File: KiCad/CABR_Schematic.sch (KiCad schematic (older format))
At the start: 22 parts, among them J1 XT60 Connector, J2 0.1\" Header, M1 Solenoid, M2 Flywheel 1, M3 Flywheel 2, Q1 PBSS4250X, SW1 Fire Mode, SW2 Microswitch, SW3 Motor Spin Up, U1 AZ1117-5.0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

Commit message: got PCB design
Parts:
- removed J1: XT60 Connector, symbol Connector_Generic:Conn_01x02
- removed M2: Flywheel 1, symbol Motor:Motor_DC_ALT
- removed M3: Flywheel 2, symbol Motor:Motor_DC_ALT
- removed SW3: Motor Spin Up, symbol Switch:SW_Push_Open
- added C3: 0.1uF, Capacitor_SMD:C_0805_2012Metric, symbol Device:C
- added J1, J5: Screw_Terminal_01x02, XT60:XT60, symbol Connector:Screw_Terminal_01x02
- added J3: Program Header, Connector_PinHeader_2.54mm:PinHeader_2x03_P2.54mm_Vertical, symbol Connector_Generic:Conn_02x03_Top_Bottom
- added J4: MicroSwitch, Connector_PinHeader_2.54mm:PinHeader_1x02_P2.54mm_Vertical, symbol Connector:Conn_01x02_Male
- C1, C2: footprint (none) -> Capacitor_SMD:C_0805_2012Metric
- D1: footprint (none) -> LED_SMD:LED_0805_2012Metric
- D2: value 1N4148 -> MMSD4148T3G; footprint Diode_THT:D_DO-35_SOD27_P7.62mm_Horizontal -> Diode_SMD:D_SOD-123
- J2: footprint (none) -> Connector_PinHeader_2.54mm:PinHeader_1x03_P2.54mm_Vertical
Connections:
- wire segments 71 -> 82
- no-connect marks 6 -> 10
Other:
- moved on the sheet: M1, SW2
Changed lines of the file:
@@
 F 0 "C2" H 6318 1896 50  0000 L CNN
 F 1 "10uF" H 6318 1805 50  0000 L CNN
-F 2 "" H 6238 1700 50  0001 C CNN
+F 2 "Capacitor_SMD:C_0805_2012Metric" H 6238 1700 50  0001 C CNN
 F 3 "~" H 6200 1850 50  0001 C CNN
 	1    6200 1850
@@
 F 0 "C1" H 5418 1896 50  0000 L CNN
 F 1 "10uF" H 5418 1805 50  0000 L CNN
-F 2 "" H 5338 1700 50  0001 C CNN
+F 2 "Capacitor_SMD:C_0805_2012Metric" H 5338 1700 50  0001 C CNN
 F 3 "~" H 5300 1850 50  0001 C CNN
 	1    5300 1850
@@
 	7100 3150 7100 3900
 Wire Wire Line
-	6050 2750 6050 2950
-Wire Wire Line
-	6050 3150 6050 2950
-Connection ~ 6050 2950
-Wire Wire Line
 	7450 4200 6750 4200
 $Comp
 L Switch:SW_Push SW2
 U 1 1 5D304392
-P 6600 3650
-F 0 "SW2" H 6600 3935 50  0000 C CNN
-F 1 "Microswitch" H 6600 3844 50  0000 C CNN
-F 2 "" H 6600 3850 50  0001 C CNN
-F 3 "~" H 6600 3850 50  0001 C CNN
-	1    6600 3650
+P 6600 3300
+F 0 "SW2" H 6600 3585 50  0000 C CNN
+F 1 "Microswitch" H 6600 3494 50  0000 C CNN
+F 2 "" H 6600 3500 50  0001 C CNN
+F 3 "~" H 6600 3500 50  0001 C CNN
+	1    6600 3300
 	1    0    0    -1
 $EndComp
@@
 	7250 2500 7250 3650
 Wire Wire Line
-	7250 3650 6800 3650
-Wire Wire Line
 	6400 3650 6400 4100
 Wire Wire Line
@@
 Wire Wire Line
 	6250 3650 6400 3650
-Connection ~ 6400 3650
 $Comp
 L Device:LED_ALT D1
@@
 F 0 "D1" H 6593 4416 50  0000 C CNN
 F 1 "Green" H 6593 4325 50  0000 C CNN
-F 2 "" H 6600 4200 50  0001 C CNN
+F 2 "LED_SMD:LED_0805_2012Metric" H 6600 4200 50  0001 C CNN
 F 3 "~" H 6600 4200 50  0001 C CNN
 	1    6600 4200
@@
 L Motor:Motor_DC_ALT M1
 U 1 1 5D318954
-P 4550 3150
-F 0 "M1" H 4697 3146 50  0000 L CNN
-F 1 "Solenoid" H 4697 3055 50  0000 L CNN
-F 2 "" H 4550 3060 50  0001 C CNN
-F 3 "~" H 4550 3060 50  0001 C CNN
-	1    4550 3150
-	1    0    0    -1
-$EndComp
-$Comp
-L Motor:Motor_DC_ALT M3
-U 1 1 5D31F859
-P 2750 2150
-F 0 "M3" V 3034 2100 50  0000 C CNN
-F 1 "Flywheel 2" V 2943 2100 50  0000 C CNN
-F 2 "" H 2750 2060 50  0001 C CNN
-F 3 "~" H 2750 2060 50  0001 C CNN
-	1    2750 2150
-	0    -1   -1   0
-$EndComp
-$Comp
-L Motor:Motor_DC_ALT M2
-U 1 1 5D31FAB2
-P 2750 1650
-F 0 "M2" V 3034 1600 50  0000 C CNN
-F 1 "Flywheel 1" V 2943 1600 50  0000 C CNN
-F 2 "" H 2750 1560 50  0001 C CNN
-F 3 "~" H 2750 1560 50  0001 C CNN
-	1    2750 1650
-	0    -1   -1   0
-$EndComp
-Wire Wire Line
-	3050 1650 3050 2150
-Wire Wire Line
-	2550 1650 2550 2150
-Wire Wire Line
-	3250 1700 3250 1400
-Wire Wire Line
-	3250 1400 2550 1400
-Wire Wire Line
-	2550 1400 2550 1650
-Connection ~ 2550 1650
-Wire Wire Line
-	3750 1700 3250 1700
-Wire Wire Line
-	4150 1700 4800 1700
-Connection ~ 4800 1700
+P 4300 3100
+F 0 "M1" H 4000 3500 50  0000 L CNN
+F 1 "Solenoid" H 3900 3600 50  0000 L CNN
+F 2 "" H 4300 3010 50  0001 C CNN
+F 3 "~" H 4300 3010 50  0001 C CNN
+	1    4300 3100
+	1    0    0    -1
+$EndComp
 Wire Wire Line
 	6450 4200 6150 4200
@@
 	0    1    1    0
 $EndComp
-$Comp
-L Switch:SW_Push_Open SW3
-U 1 1 5D32C4C6
-P 3950 1700
-F 0 "SW3" H 3950 1915 50  0000 C CNN
-F 1 "Motor Spin Up" H 3950 1824 50  0000 C CNN
-F 2 "" H 3950 1900 50  0001 C CNN
-F 3 "~" H 3950 1900 50  0001 C CNN
-	1    3950 1700
-	1    0    0    -1
-$EndComp
-Wire Wire Line
-	4550 3450 4550 3500
 Wire Wire Line
 	5950 3650 5750 3650
@@
 L power:GND #PWR04
 U 1 1 5D36C3A6
-P 5700 2950
-F 0 "#PWR04" H 5700 2700 50  0001 C CNN
-F 1 "GND" V 5705 2822 50  0000 R CNN
-F 2 "" H 5700 2950 50  0001 C CNN
-F 3 "" H 5700 2950 50  0001 C CNN
-	1    5700 2950
-	0    1    1    0
-$EndComp
-Wire Wire Line
-	5700 2950 6050 2950
+P 6050 3150
+F 0 "#PWR04" H 6050 2900 50  0001 C CNN
+F 1 "GND" H 6100 3000 50  0000 R CNN
+F 2 "" H 6050 3150 50  0001 C CNN
+F 3 "" H 6050 3150 50  0001 C CNN
+	1    6050 3150
+	1    0    0    -1
+$EndComp
 $Comp
 L power:GND #PWR03
 U 1 1 5D36E3F2
-P 5000 3000
-F 0 "#PWR03" H 5000 2750 50  0001 C CNN
-F 1 "GND" V 5005 2872 50  0000 R CNN
-F 2 "" H 5000 3000 50  0001 C CNN
-F 3 "" H 5000 3000 50  0001 C CNN
-	1    5000 3000
-	0    -1   -1   0
-$EndComp
-Wire Wire Line
-	5000 3000 4950 3000
-$Comp
-L power:GND #PWR01
-U 1 1 5D372C94
-P 3050 2350
-F 0 "#PWR01" H 3050 2100 50  0001 C CNN
-F 1 "GND" H 3055 2177 50  0000 C CNN
-F 2 "" H 3050 2350 50  0001 C CNN
-F 3 "" H 3050 2350 50  0001 C CNN
-	1    3050 2350
-	1    0    0    -1
-$EndComp
-Wire Wire Line
-	3050 2150 3050 2350
-Connection ~ 3050 2150
+P 4950 3000
+F 0 "#PWR03" H 4950 2750 50  0001 C CNN
+F 1 "GND" H 5200 2950 50  0000 R CNN
+F 2 "" H 4950 3000 50  0001 C CNN
+F 3 "" H 4950 3000 50  0001 C CNN
+	1    4950 3000
+	1    0    0    -1
+$EndComp
 $Comp
 L power:GND #PWR05
@@
 Connection ~ 5700 3800
 Wire Wire Line
-	5700 3800 7450 3800
+	5700 3800 7400 3800
 $Comp
 L Diode:1N4148 D2
 U 1 1 5D2EE859
 P 4050 3200
-F 0 "D2" V 4004 3279 50  0000 L CNN
-F 1 "1N4148" V 4095 3279 50  0000 L CNN
-F 2 "Diode_THT:D_DO-35_SOD27_P7.62mm_Horizontal" H 4050 3025 50  0001 C CNN
+F 0 "D2" V 3950 2900 50  0000 L CNN
+F 1 "MMSD4148T3G" V 4050 2550 50  0000 L CNN
+F 2 "Diode_SMD:D_SOD-123" H 4050 3025 50  0001 C CNN
 F 3 "https://assets.nexperia.com/documents/data-sheet/1N4148_1N4448.pdf" H 4050 3200 50  0001 C CNN
 	1    4050 3200
@@
 	4050 2800 4050 3050
 Connection ~ 4550 2800
-Wire Wire Line
-	4550 2800 4550 2950
 Wire Wire Line
 	4050 3350 4050 3500
@@
 Connection ~ 7600 2400
 Wire Wire Line
-	7600 2500 7600 3500
-Wire Wire Line
-	7600 3500 8050 3500
+	7600 2500 7600 3300
 Connection ~ 7600 2500
 $Comp
@@
 $EndComp
 Wire Wire Line
-	8050 4700 8050 4950
+	8050 4700 8050 4900
 $Comp
 L MCU_Microchip_ATtiny:ATtiny85-20SU U2
@@
 F 0 "J2" V 7362 2344 50  0000 L CNN
 F 1 "0.1\" Header" V 7350 1550 50  0000 L CNN
-F 2 "" H 7300 2200 50  0001 C CNN
+F 2 "Connector_PinHeader_2.54mm:PinHeader_1x03_P2.54mm_Vertical" H 7300 2200 50  0001 C CNN
 F 3 "~" H 7300 2200 50  0001 C CNN
 	1    7300 2200
@@
 NoConn ~ 7100 2050
 NoConn ~ 7500 1950
-$Comp
-L Connector_Generic:Conn_01x02 J1
-U 1 1 5D39BE5A
-P 5000 2650
-F 0 "J1" H 5080 2642 50  0000 L CNN
-F 1 "XT60 Connector" H 5080 2551 50  0000 L CNN
-F 2 "" H 5000 2650 50  0001 C CNN
-F 3 "~" H 5000 2650 50  0001 C CNN
-	1    5000 2650
-	1    0    0    -1
-$EndComp
 Wire Wire Line
 	4800 2750 4800 3000
@@
 Wire Wire Line
 	5750 2000 6200 2000
+$Comp
+L Connector_Generic:Conn_02x03_Top_Bottom J3
+U 1 1 5D387500
+P 6950 4800
+F 0 "J3" H 7000 5117 50  0000 C CNN
+F 1 "Program Header" H 7000 5026 50  0000 C CNN
+F 2 "Connector_PinHeader_2.54mm:PinHeader_2x03_P2.54mm_Vertical" H 6950 4800 50  0001 C CNN
+F 3 "~" H 6950 4800 50  0001 C CNN
+	1    6950 4800
+	1    0    0    -1
+$EndComp
+Wire Wire Line
+	7250 4700 7300 4700
+Wire Wire Line
+	7300 4700 7300 3500
+Wire Wire Line
+	7300 3500 7600 3500
+Wire Wire Line
+	7250 4900 8050 4900
+Connection ~ 8050 4900
+Wire Wire Line
+	8050 4900 8050 4950
+Wire Wire Line
+	6750 4900 6400 4900
+Wire Wire Line
+	6400 4900 6400 4300
+Wire Wire Line
+	6400 4300 7450 4300
+Wire Wire Line
+	7250 4800 7400 4800
+Wire Wire Line
+	7400 4800 7400 3800
+Connection ~ 7400 3800
+Wire Wire Line
+	7400 3800 7450 3800
+Wire Wire Line
+	7100 3900 7100 4450
+Wire Wire Line
+	7100 4450 6550 4450
+Wire Wire Line
+	6550 4450 6550 4700
+Wire Wire Line
+	6550 4700 6750 4700
+Connection ~ 7100 3900
+Wire Wire Line
+	6950 4000 6950 4400
+Wire Wire Line
+	6950 4400 6500 4400
+Wire Wire Line
+	6500 4400 6500 4800
+Wire Wire Line
+	6500 4800 6750 4800
+Connection ~ 6950 4000
+Wire Wire Line
+	6050 2750 6050 3150
+Connection ~ 6050 3150
+$Comp
+L Connector:Conn_01x02_Male J4
+U 1 1 5D3A2F3D
+P 6650 3450
+F 0 "J4" V 6712 3494 50  0000 L CNN
+F 1 "MicroSwitch" V 6600 3200 50  0000 L CNN
+F 2 "Connector_PinHeader_2.54mm:PinHeader_1x02_P2.54mm_Vertical" H 6650 3450 50  0001 C CNN
+F 3 "~" H 6650 3450 50  0001 C CNN
+	1    6650 3450
+	0    1    1    0
+$EndComp
+Wire Wire Line
+	6650 3650 7250 3650
+Wire Wire Line
+	6550 3650 6400 3650
+Connection ~ 6400 3650
+NoConn ~ 6800 3300
+NoConn ~ 6400 3300
+$Comp
+L Connector:Screw_Terminal_01x02 J1
+U 1 1 5D3AE752
+P 4750 3150
+F 0 "J1" H 4830 3142 50  0000 L CNN
+F 1 "Screw_Terminal_01x02" H 4830 3051 50  0000 L CNN
+F 2 "XT60:XT60" H 4750 3150 50  0001 C CNN
+F 3 "~" H 4750 3150 50  0001 C CNN
+	1    4750 3150
+	1    0    0    -1
+$EndComp
+Wire Wire Line
+	4550 3250 4550 3500
+Wire Wire Line
+	4550 2800 4550 3150
+$Comp
+L Connector:Screw_Terminal_01x02 J5
+U 1 1 5D3B2F49
+P 5000 2650
+F 0 "J5" H 5080 2642 50  0000 L CNN
+F 1 "Screw_Terminal_01x02" H 5080 2551 50  0000 L CNN
+F 2 "XT60:XT60" H 5000 2650 50  0001 C CNN
+F 3 "~" H 5000 2650 50  0001 C CNN
+	1    5000 2650
+	1    0    0    -1
+$EndComp
+NoConn ~ 4300 2900
+NoConn ~ 4300 3400
+$Comp
+L Device:C C3
+U 1 1 5D3EBA09
+P 7900 3300
+F 0 "C3" V 7648 3300 50  0000 C CNN
+F 1 "0.1uF" V 7739 3300 50  0000 C CNN
+F 2 "Capacitor_SMD:C_0805_2012Metric" H 7938 3150 50  0001 C CNN
+F 3 "~" H 7900 3300 50  0001 C CNN
+	1    7900 3300
+	0    1    1    0
+$EndComp
+Wire Wire Line
+	8050 3300 8050 3500
+Wire Wire Line
+	7750 3300 7600 3300
+Connection ~ 7600 3300
+Wire Wire Line
+	7600 3300 7600 3500
 $EndSCHEMATC

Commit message: redid file structure
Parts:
- J1, J5: value Screw_Terminal_01x02 -> XT60
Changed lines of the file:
@@
 P 4750 3150
 F 0 "J1" H 4830 3142 50  0000 L CNN
-F 1 "Screw_Terminal_01x02" H 4830 3051 50  0000 L CNN
+F 1 "XT60" H 4830 3051 50  0000 L CNN
 F 2 "XT60:XT60" H 4750 3150 50  0001 C CNN
 F 3 "~" H 4750 3150 50  0001 C CNN
@@
 P 5000 2650
 F 0 "J5" H 5080 2642 50  0000 L CNN
-F 1 "Screw_Terminal_01x02" H 5080 2551 50  0000 L CNN
+F 1 "XT60" H 5080 2551 50  0000 L CNN
 F 2 "XT60:XT60" H 5000 2650 50  0001 C CNN
 F 3 "~" H 5000 2650 50  0001 C CNN

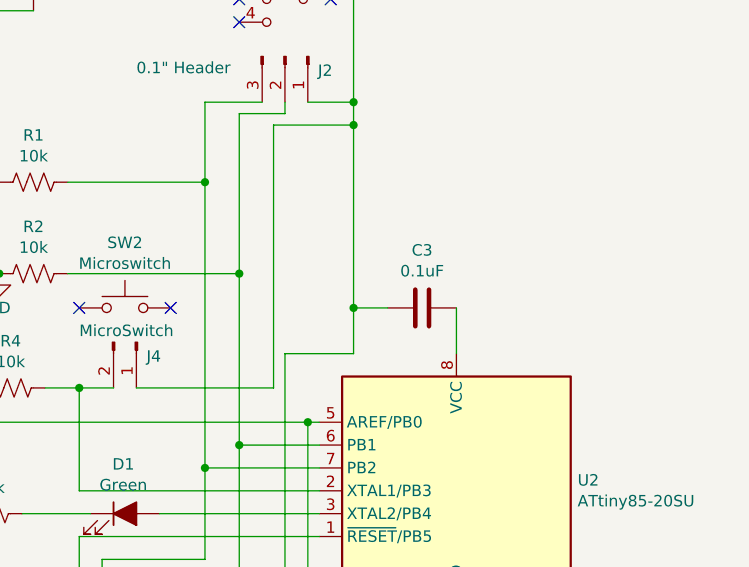
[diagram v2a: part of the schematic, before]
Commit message: updated design and fixed output pins
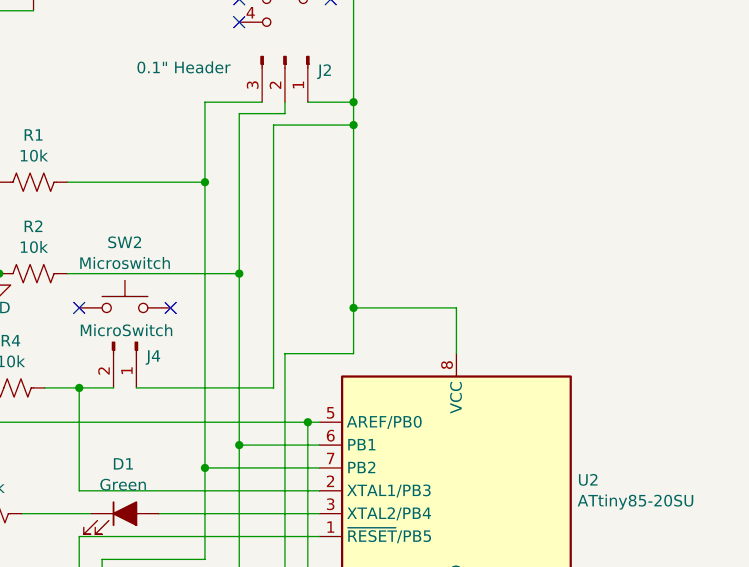
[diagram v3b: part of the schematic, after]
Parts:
- removed C3: 0.1uF, Capacitor_SMD:C_0805_2012Metric, symbol Device:C
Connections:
- net at C2.1, J2.1 (Pin_1), J3.4 (Pin_4)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: now also U2.8 (VCC)
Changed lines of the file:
@@
 NoConn ~ 4300 2900
 NoConn ~ 4300 3400
-$Comp
-L Device:C C3
-U 1 1 5D3EBA09
-P 7900 3300
-F 0 "C3" V 7648 3300 50  0000 C CNN
-F 1 "0.1uF" V 7739 3300 50  0000 C CNN
-F 2 "Capacitor_SMD:C_0805_2012Metric" H 7938 3150 50  0001 C CNN
-F 3 "~" H 7900 3300 50  0001 C CNN
-	1    7900 3300
-	0    1    1    0
-$EndComp
 Wire Wire Line
 	8050 3300 8050 3500
-Wire Wire Line
-	7750 3300 7600 3300
 Connection ~ 7600 3300
 Wire Wire Line
 	7600 3300 7600 3500
+Wire Wire Line
+	7600 3300 8050 3300
 $EndSCHEMATC

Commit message: more board updates
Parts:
- added C3: 0.1uF, Capacitor_SMD:C_0805_2012Metric, symbol Device:C
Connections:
- net GND: now also C3.2
- net at C2.1, J2.1 (Pin_1), J3.4 (Pin_4)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: now also C3.1
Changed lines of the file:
@@
 Wire Wire Line
 	7600 3300 8050 3300
+$Comp
+L Device:C C3
+U 1 1 5D5D8A62
+P 8650 3300
+F 0 "C3" V 8902 3300 50  0000 C CNN
+F 1 "0.1uF" V 8811 3300 50  0000 C CNN
+F 2 "Capacitor_SMD:C_0805_2012Metric" H 8688 3150 50  0001 C CNN
+F 3 "~" H 8650 3300 50  0001 C CNN
+	1    8650 3300
+	0    -1   -1   0
+$EndComp
+$Comp
+L power:GND #PWR0101
+U 1 1 5D5D9924
+P 9000 3300
+F 0 "#PWR0101" H 9000 3050 50  0001 C CNN
+F 1 "GND" V 9005 3172 50  0000 R CNN
+F 2 "" H 9000 3300 50  0001 C CNN
+F 3 "" H 9000 3300 50  0001 C CNN
+	1    9000 3300
+	0    -1   -1   0
+$EndComp
+Wire Wire Line
+	8050 3300 8500 3300
+Connection ~ 8050 3300
+Wire Wire Line
+	8800 3300 9000 3300
 $EndSCHEMATC

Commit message: more modifications
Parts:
- Q1: symbol Device:Q_NPN_ECB -> Device:Q_NPN_Darlington_BCE
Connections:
- net GND: now also Q1.3 (E); no longer Q1.1 (E)
- net at R5.2, R6.2, U2.5 (AREF/PB0): now also J3.4 (Pin_4); no longer J3.5 (Pin_5)
- net at C2.1, C3.1, J2.1 (Pin_1)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: now also J3.2 (Pin_2); no longer J3.4 (Pin_4)
- net at J2.3 (Pin_3), R1.2, U2.7 (PB2): now also J3.3 (Pin_3); no longer J3.2 (Pin_2)
- net at U2.1 (~RESET~/PB5): now also J3.5 (Pin_5); no longer J3.3 (Pin_3)
- net at R6.1: now also Q1.1 (B); no longer Q1.3 (B)
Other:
- moved on the sheet: J3
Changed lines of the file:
@@
 	7100 2450 7100 3150
 Wire Wire Line
-	7100 3900 7450 3900
-Wire Wire Line
 	6950 2400 6950 2750
 Wire Wire Line
-	6950 4000 7450 4000
+	6950 4000 7150 4000
 Wire Wire Line
 	6350 2750 6950 2750
@@
 Wire Wire Line
 	7100 3150 7100 3900
-Wire Wire Line
-	7450 4200 6750 4200
 $Comp
 L Switch:SW_Push SW2
@@
 $EndComp
 Connection ~ 5700 3800
-Wire Wire Line
-	5700 3800 7400 3800
 $Comp
 L Diode:1N4148 D2
@@
 	1    0    0    -1
 $EndComp
-Wire Wire Line
-	8050 4700 8050 4900
 $Comp
 L MCU_Microchip_ATtiny:ATtiny85-20SU U2
@@
 $EndComp
 $Comp
-L Device:Q_NPN_ECB Q1
+L Device:Q_NPN_Darlington_BCE Q1
 U 1 1 5D37E1CE
 P 4850 3950
@@
 	5300 3800 5050 3800
 Wire Wire Line
-	5050 3800 5050 3950
-Wire Wire Line
 	4550 3500 4750 3500
 Wire Wire Line
 	4750 3500 4750 3750
 Connection ~ 4550 3500
-Wire Wire Line
-	4750 4150 5700 4150
 Connection ~ 5700 4150
 Wire Wire Line
@@
 Wire Wire Line
 	5750 2000 6200 2000
-$Comp
-L Connector_Generic:Conn_02x03_Top_Bottom J3
-U 1 1 5D387500
-P 6950 4800
-F 0 "J3" H 7000 5117 50  0000 C CNN
-F 1 "Program Header" H 7000 5026 50  0000 C CNN
-F 2 "Connector_PinHeader_2.54mm:PinHeader_2x03_P2.54mm_Vertical" H 6950 4800 50  0001 C CNN
-F 3 "~" H 6950 4800 50  0001 C CNN
-	1    6950 4800
-	1    0    0    -1
-$EndComp
-Wire Wire Line
-	7250 4700 7300 4700
-Wire Wire Line
-	7300 4700 7300 3500
-Wire Wire Line
-	7300 3500 7600 3500
-Wire Wire Line
-	7250 4900 8050 4900
-Connection ~ 8050 4900
-Wire Wire Line
-	8050 4900 8050 4950
-Wire Wire Line
-	6750 4900 6400 4900
-Wire Wire Line
-	6400 4900 6400 4300
-Wire Wire Line
-	6400 4300 7450 4300
-Wire Wire Line
-	7250 4800 7400 4800
-Wire Wire Line
-	7400 4800 7400 3800
-Connection ~ 7400 3800
-Wire Wire Line
-	7400 3800 7450 3800
-Wire Wire Line
-	7100 3900 7100 4450
-Wire Wire Line
-	7100 4450 6550 4450
-Wire Wire Line
-	6550 4450 6550 4700
-Wire Wire Line
-	6550 4700 6750 4700
-Connection ~ 7100 3900
-Wire Wire Line
-	6950 4000 6950 4400
-Wire Wire Line
-	6950 4400 6500 4400
-Wire Wire Line
-	6500 4400 6500 4800
-Wire Wire Line
-	6500 4800 6750 4800
-Connection ~ 6950 4000
 Wire Wire Line
 	6050 2750 6050 3150
@@
 Wire Wire Line
 	8050 3300 8050 3500
-Connection ~ 7600 3300
-Wire Wire Line
-	7600 3300 7600 3500
 Wire Wire Line
 	7600 3300 8050 3300
@@
 Wire Wire Line
 	8800 3300 9000 3300
+Wire Wire Line
+	5050 3800 5050 3950
+Wire Wire Line
+	4750 4150 5700 4150
+Wire Wire Line
+	5700 3800 7300 3800
+Wire Wire Line
+	8050 4700 8050 4850
+$Comp
+L Connector_Generic:Conn_02x03_Top_Bottom J3
+U 1 1 5D387500
+P 7200 4900
+F 0 "J3" H 7250 5217 50  0000 C CNN
+F 1 "Program Header" H 7250 5126 50  0000 C CNN
+F 2 "Connector_PinHeader_2.54mm:PinHeader_2x03_P2.54mm_Vertical" H 7200 4900 50  0001 C CNN
+F 3 "~" H 7200 4900 50  0001 C CNN
+	1    7200 4900
+	1    0    0    -1
+$EndComp
+Wire Wire Line
+	7600 3300 6900 3300
+Wire Wire Line
+	6900 3300 6900 4900
+Wire Wire Line
+	6900 4900 7000 4900
+Connection ~ 7600 3300
+Wire Wire Line
+	7000 5000 6750 5000
+Wire Wire Line
+	6750 5000 6750 4450
+Wire Wire Line
+	6750 4450 7150 4450
+Wire Wire Line
+	6750 4200 7450 4200
+Wire Wire Line
+	7150 4450 7150 4000
+Connection ~ 7150 4000
+Wire Wire Line
+	7150 4000 7450 4000
+Wire Wire Line
+	7500 4800 7500 4400
+Wire Wire Line
+	7500 4400 7300 4400
+Wire Wire Line
+	7300 4400 7300 3800
+Connection ~ 7300 3800
+Wire Wire Line
+	7300 3800 7450 3800
+Wire Wire Line
+	7500 4900 7700 4900
+Wire Wire Line
+	7700 4900 7700 4700
+Wire Wire Line
+	7700 4700 7450 4700
+Wire Wire Line
+	7450 4700 7450 4300
+Wire Wire Line
+	7500 5000 7850 5000
+Wire Wire Line
+	7850 5000 7850 4850
+Wire Wire Line
+	7850 4850 8050 4850
+Connection ~ 8050 4850
+Wire Wire Line
+	8050 4850 8050 4950
+Wire Wire Line
+	7000 4800 7000 3900
+Wire Wire Line
+	7000 3900 7100 3900
+Connection ~ 7100 3900
+Wire Wire Line
+	7100 3900 7450 3900
 $EndSCHEMATC

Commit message: more fixes
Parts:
- Q1: value PBSS4250X -> FQP30N06L; symbol Device:Q_NPN_Darlington_BCE -> Device:Q_NPN_Darlington_BEC
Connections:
- net GND: now also Q1.2 (E); no longer Q1.3 (E)
- net at D2.2 (A), J1.2 (Pin_2): now also Q1.3 (C); no longer Q1.2 (C)
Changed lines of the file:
@@
 $EndComp
 $Comp
-L Device:Q_NPN_Darlington_BCE Q1
+L Device:Q_NPN_Darlington_BEC Q1
 U 1 1 5D37E1CE
 P 4850 3950
 F 0 "Q1" H 5041 3996 50  0000 L CNN
-F 1 "PBSS4250X" H 5041 3905 50  0000 L CNN
+F 1 "FQP30N06L" H 5041 3905 50  0000 L CNN
 F 2 "Package_TO_SOT_SMD:SOT-89-3" H 5050 4050 50  0001 C CNN
 F 3 "https://assets.nexperia.com/documents/data-sheet/PBSS4250X.pdf" H 4850 3950 50  0001 C CNN

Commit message: update schematic
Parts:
- Q1: footprint Package_TO_SOT_SMD:SOT-89-3 -> Package_TO_SOT_THT:TO-220-3_Vertical
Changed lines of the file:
@@
 EESchema Schematic File Version 4
 LIBS:CABR_Schematic-cache
-EELAYER 29 0
+EELAYER 30 0
 EELAYER END
 $Descr A4 11693 8268
@@
 F 0 "Q1" H 5041 3996 50  0000 L CNN
 F 1 "FQP30N06L" H 5041 3905 50  0000 L CNN
-F 2 "Package_TO_SOT_SMD:SOT-89-3" H 5050 4050 50  0001 C CNN
+F 2 "Package_TO_SOT_THT:TO-220-3_Vertical" H 5050 4050 50  0001 C CNN
 F 3 "https://assets.nexperia.com/documents/data-sheet/PBSS4250X.pdf" H 4850 3950 50  0001 C CNN
 	1    4850 3950

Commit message: more updates
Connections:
- net at J3.4 (Pin_4), R5.2, U2.5 (AREF/PB0): now also R6.1; no longer R6.2
- net at Q1.1 (B): now also R6.2; no longer R6.1
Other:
- moved on the sheet: R6
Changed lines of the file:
@@
 EESchema Schematic File Version 4
 LIBS:CABR_Schematic-cache
-EELAYER 30 0
+EELAYER 29 0
 EELAYER END
 $Descr A4 11693 8268
@@
 Wire Wire Line
 	4800 2400 4550 2400
-Wire Wire Line
-	4550 2400 4550 2800
 Connection ~ 4800 2400
 Wire Wire Line
@@
 L Device:R_US R6
 U 1 1 5D38E3F6
-P 5450 3800
-F 0 "R6" V 5655 3800 50  0000 C CNN
-F 1 "1k" V 5564 3800 50  0000 C CNN
-F 2 "Resistor_SMD:R_0805_2012Metric" V 5490 3790 50  0001 C CNN
-F 3 "~" H 5450 3800 50  0001 C CNN
-	1    5450 3800
-	0    -1   -1   0
+P 5250 3850
+F 0 "R6" V 5455 3850 50  0000 C CNN
+F 1 "1k" V 5364 3850 50  0000 C CNN
+F 2 "Resistor_SMD:R_0805_2012Metric" V 5290 3840 50  0001 C CNN
+F 3 "~" H 5250 3850 50  0001 C CNN
+	1    5250 3850
+	0    1    1    0
 $EndComp
 Wire Wire Line
@@
 	5700 4200 5750 4200
 Wire Wire Line
-	5300 3800 5050 3800
-Wire Wire Line
 	4550 3500 4750 3500
 Wire Wire Line
@@
 U 1 1 5D3AE752
 P 4750 3150
-F 0 "J1" H 4830 3142 50  0000 L CNN
-F 1 "XT60" H 4830 3051 50  0000 L CNN
+F 0 "J1" H 4700 2950 50  0000 L CNN
+F 1 "XT60" H 4650 2850 50  0000 L CNN
 F 2 "XT60:XT60" H 4750 3150 50  0001 C CNN
 F 3 "~" H 4750 3150 50  0001 C CNN
@@
 	8800 3300 9000 3300
 Wire Wire Line
-	5050 3800 5050 3950
-Wire Wire Line
 	4750 4150 5700 4150
 Wire Wire Line
@@
 Wire Wire Line
 	7100 3900 7450 3900
+Wire Wire Line
+	5600 3800 5600 3850
+Wire Wire Line
+	5600 3850 5400 3850
+Wire Wire Line
+	4550 2400 4550 2800
+Wire Wire Line
+	5100 3850 5050 3850
+Wire Wire Line
+	5050 3850 5050 3950
 $EndSCHEMATC
